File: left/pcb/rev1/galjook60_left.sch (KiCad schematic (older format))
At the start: 88 parts

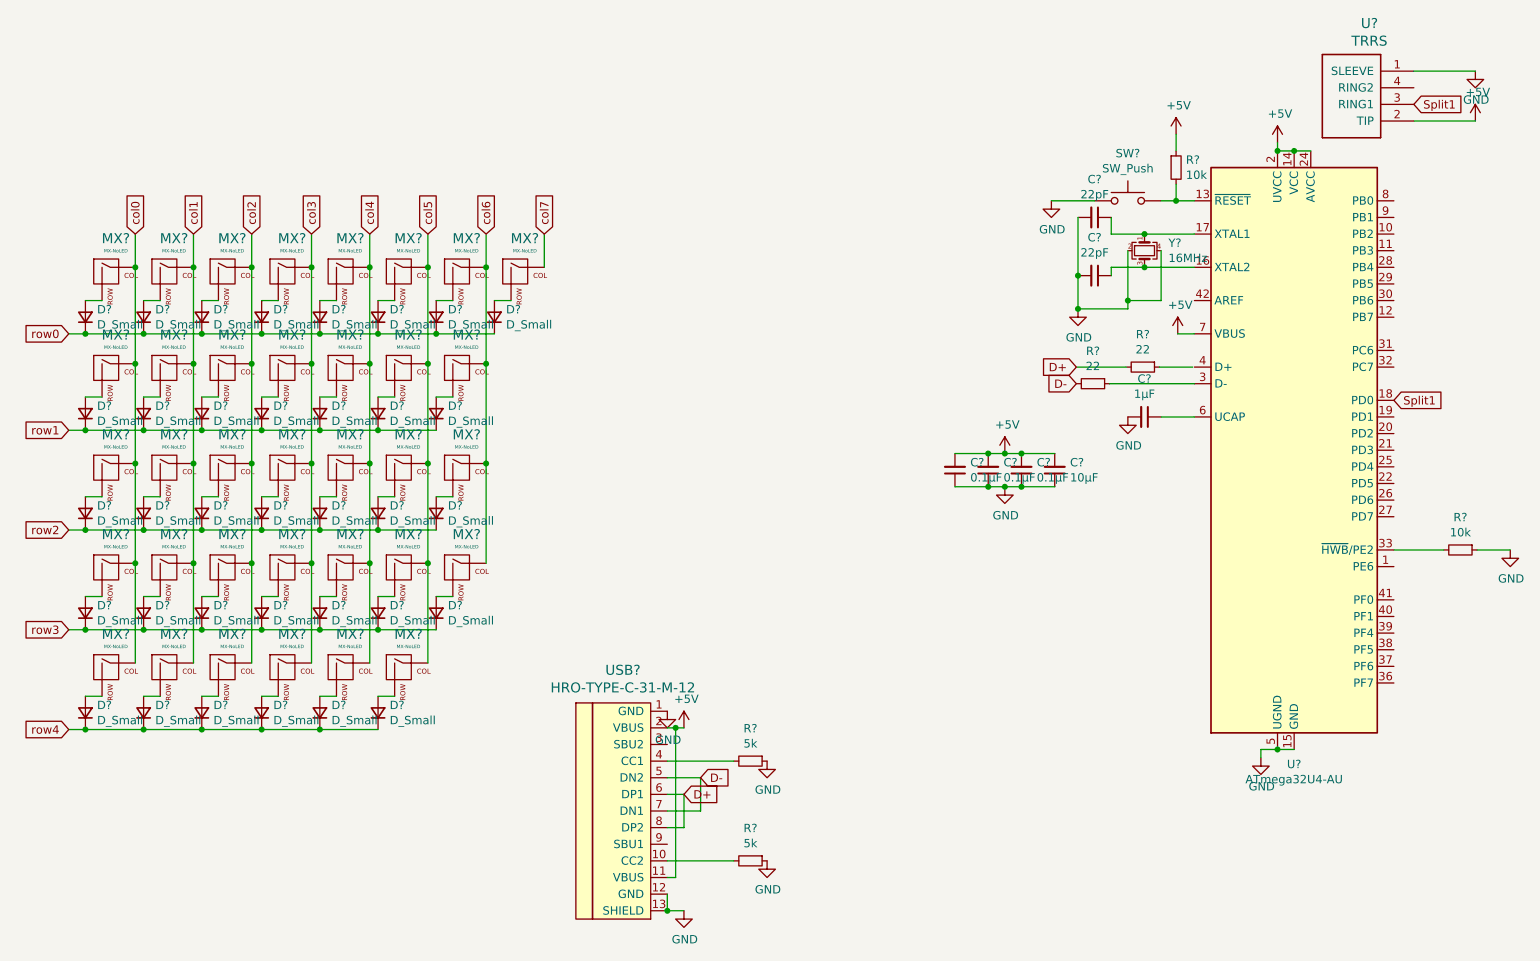
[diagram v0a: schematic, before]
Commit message: Routed most of the pcb for the left half
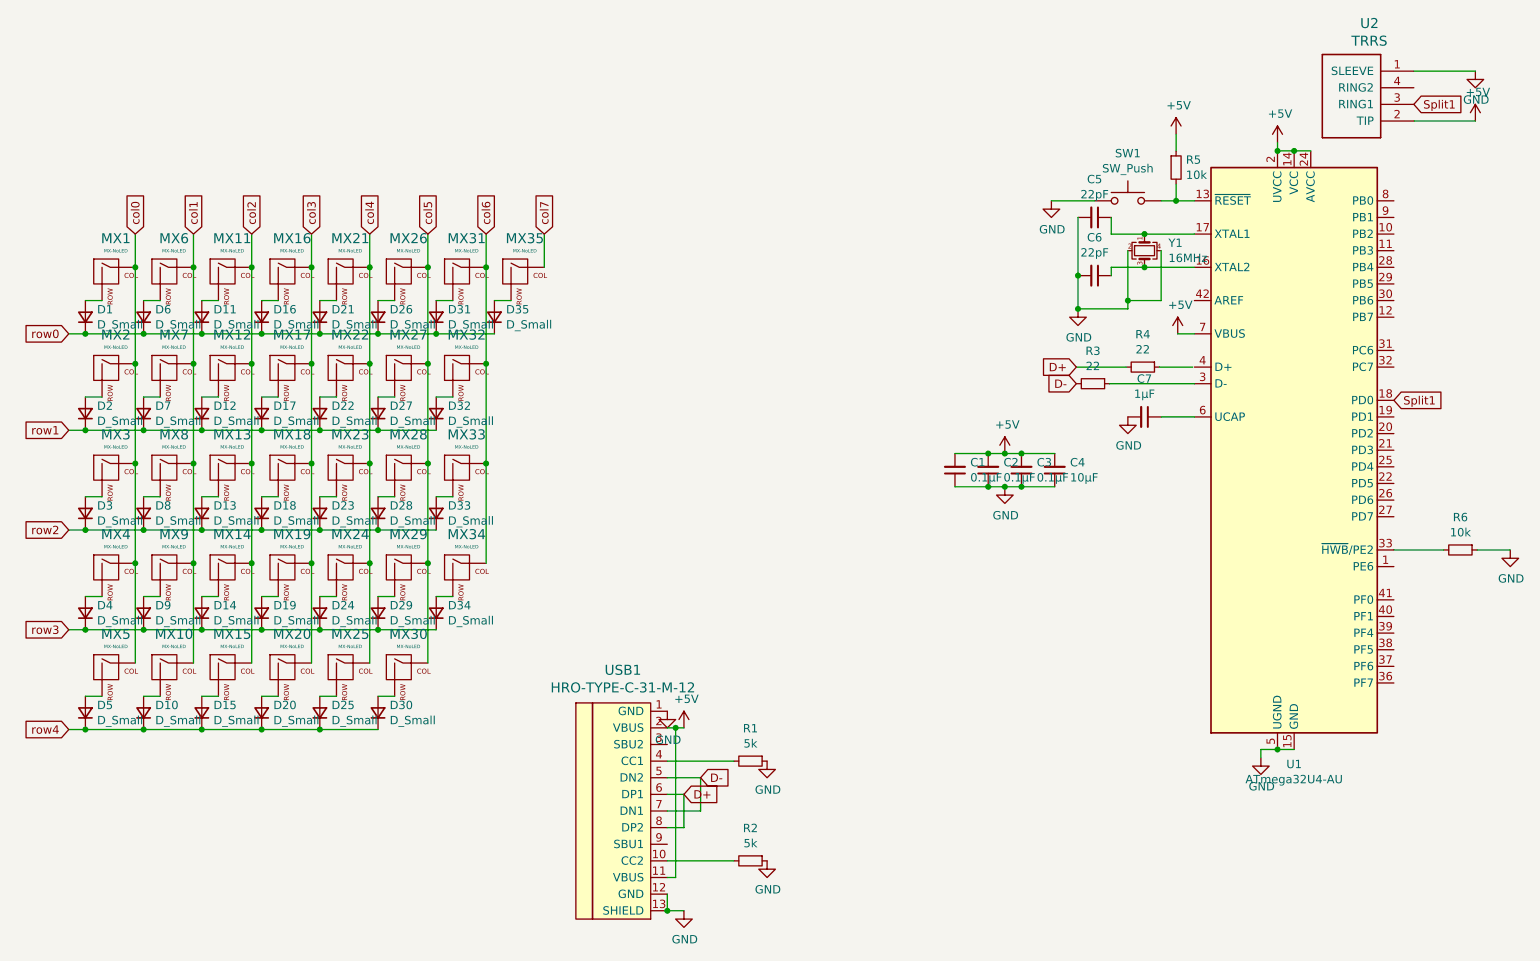
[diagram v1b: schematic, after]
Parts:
- C1, C2, C3, C4, C5, C6, C7: renamed from C?; footprint (none) -> Capacitor_SMD:C_0805_2012Metric
- D1, D10, D11, D12, D13, D14, D15, D16, D17, D18, D19, D2, D20, D21, D22, D23, D24, D25, D26, D27, D28, D29, D3, D30, D31, D32, D33, D34, D35, D4, D5, D6, D7, D8, D9: renamed from D?; footprint (none) -> Diode_SMD:D_SOD-123
- MX1, MX11, MX12, MX13, MX14, MX16, MX17, MX18, MX19, MX21, MX22, MX23, MX24, MX26, MX27, MX28, MX29, MX31, MX32, MX33, MX34, MX35, MX6, MX7, MX8, MX9: renamed from MX?; footprint (none) -> MX_Only:MXOnly-1U
- MX10, MX15, MX20, MX30, MX5: renamed from MX?; footprint (none) -> MX_Only:MXOnly-1.25U
- MX2: renamed from MX?; footprint (none) -> MX_Only:MXOnly-1.5U
- MX25: renamed from MX?; footprint (none) -> MX_Only:MXOnly-2U
- MX3: renamed from MX?; footprint (none) -> MX_Only:MXOnly-1.75U
- MX4: renamed from MX?; footprint (none) -> MX_Only:MXOnly-2.25U
- R1, R2, R3, R4, R5, R6: renamed from R?; footprint (none) -> Resistor_SMD:R_0805_2012Metric
- SW1: renamed from SW?; footprint (none) -> random-keyboard-parts:SKQG-1155865
- U2: renamed from U?; footprint (none) -> Keebio-Parts:TRRS_Jack
- USB1: renamed from USB?; footprint (none) -> Keebio-Parts:HRO-TYPE-C-31-M-12-Assembly
- Y1: renamed from Y?; footprint (none) -> Crystal:Crystal_SMD_3225-4Pin_3.2x2.5mm
- gave numbers to parts that had none: 1

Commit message: Finalized PCB for the left side
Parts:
- MX1, MX11, MX12, MX13, MX14, MX16, MX17, MX18, MX19, MX21, MX22, MX23, MX24, MX26, MX27, MX28, MX29, MX31, MX32, MX33, MX34, MX35, MX6, MX7, MX8, MX9: footprint MX_Only:MXOnly-1U -> MX_Only:MXOnly-1U-NoLED
- MX10, MX15, MX20, MX30, MX5: footprint MX_Only:MXOnly-1.25U -> MX_Only:MXOnly-1.25U-NoLED
- MX2: footprint MX_Only:MXOnly-1.5U -> MX_Only:MXOnly-1.5U-NoLED
- MX25: footprint MX_Only:MXOnly-2U -> MX_Only:MXOnly-2U-NoLED
- MX3: footprint MX_Only:MXOnly-1.75U -> MX_Only:MXOnly-1.75U-NoLED
- MX4: footprint MX_Only:MXOnly-2.25U -> MX_Only:MXOnly-2.25U-NoLED
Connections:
- net GND: now also U2.4 (RING2); no longer U2.1 (SLEEVE)
- net Split1: now also U1.22 (PD5); no longer U1.18 (PD0)
- net col0: now also U1.1 (PE6)
- net col1: now also U1.18 (PD0)
- net col2: now also U1.25 (PD4)
- net col3: now also U1.26 (PD6)
- net col4: now also U1.27 (PD7)
- net col5: now also U1.19 (PD1)
- net col6: now also U1.38 (PF5)
- net col7: now also U1.30 (PB6)
- net row0: now also U1.12 (PB7)
- net row1: now also U1.11 (PB3)
- net row2: now also U1.41 (PF0)
- net row3: now also U1.40 (PF1)
- net row4: now also U1.39 (PF4)
- net at U1.4 (D+): now also R4.1

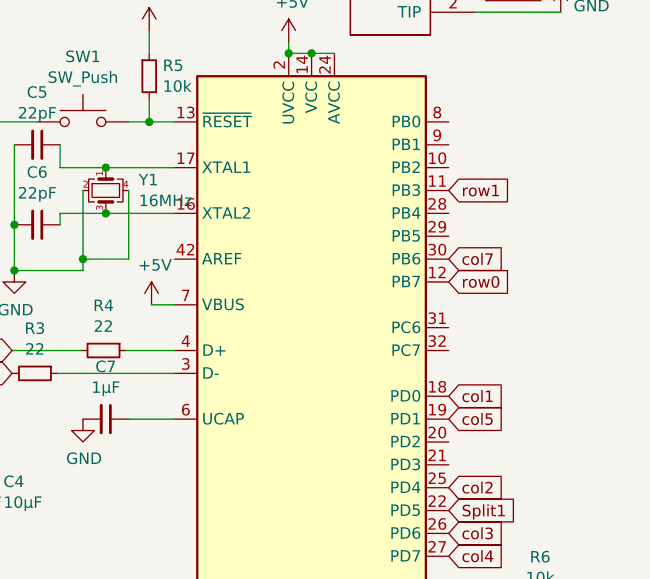
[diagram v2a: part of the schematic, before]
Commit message: Added schematic for the PCB for the right side
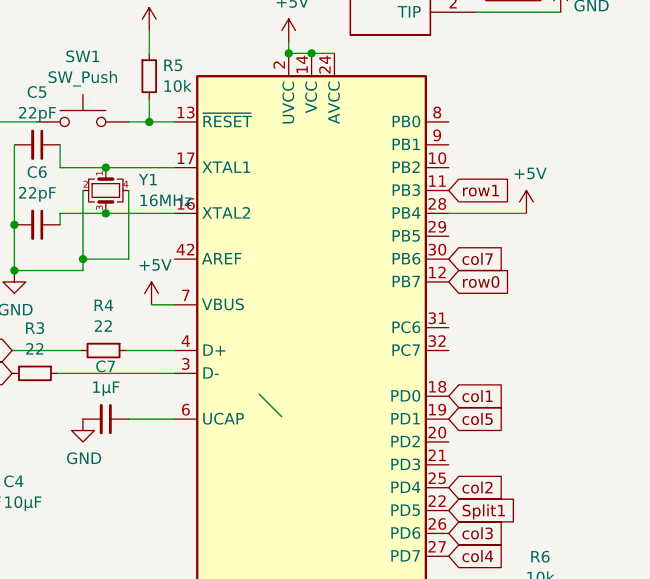
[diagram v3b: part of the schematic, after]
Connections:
- net +5V: now also U1.28 (PB4)
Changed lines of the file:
@@
 Text GLabel 10330 3500 2    50   Input ~ 0
 col1
+Entry Wire Line
+	9500 3490 9600 3590
+Wire Wire Line
+	10330 2700 10670 2700
+$Comp
+L power:+5V #PWR?
+U 1 1 607EC16E
+P 10670 2700
+F 0 "#PWR?" H 10670 2550 50  0001 C CNN
+F 1 "+5V" H 10685 2873 50  0000 C CNN
+F 2 "" H 10670 2700 50  0001 C CNN
+F 3 "" H 10670 2700 50  0001 C CNN
+	1    10670 2700
+	1    0    0    -1
+$EndComp
 $EndSCHEMATC

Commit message: updated left side PCB to reflect other split keyboards
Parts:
- MX25: footprint MX_Only:MXOnly-2U-NoLED -> MX_Only:MXOnly-2.25U-NoLED
- MX30: footprint MX_Only:MXOnly-1.25U-NoLED -> MX_Only:MXOnly-1U-NoLED
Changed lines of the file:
@@
 F 0 "MX25" H 4053 5353 60  0000 C CNN
 F 1 "MX-NoLED" H 4053 5279 20  0000 C CNN
-F 2 "MX_Only:MXOnly-2U-NoLED" H 3395 5105 60  0001 C CNN
+F 2 "MX_Only:MXOnly-2.25U-NoLED" H 3395 5105 60  0001 C CNN
 F 3 "" H 3395 5105 60  0001 C CNN
 	1    4020 5130
@@
 F 0 "MX30" H 4403 5353 60  0000 C CNN
 F 1 "MX-NoLED" H 4403 5279 20  0000 C CNN
-F 2 "MX_Only:MXOnly-1.25U-NoLED" H 3745 5105 60  0001 C CNN
+F 2 "MX_Only:MXOnly-1U-NoLED" H 3745 5105 60  0001 C CNN
 F 3 "" H 3745 5105 60  0001 C CNN
 	1    4370 5130
